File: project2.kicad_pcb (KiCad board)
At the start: 2 copper layers, 15 parts, among them J1 USB_C_Receptacle_PowerOnly_6P, Q1 FS8205A, Q2 DW01A, U1 TP4056-42-ESOP8

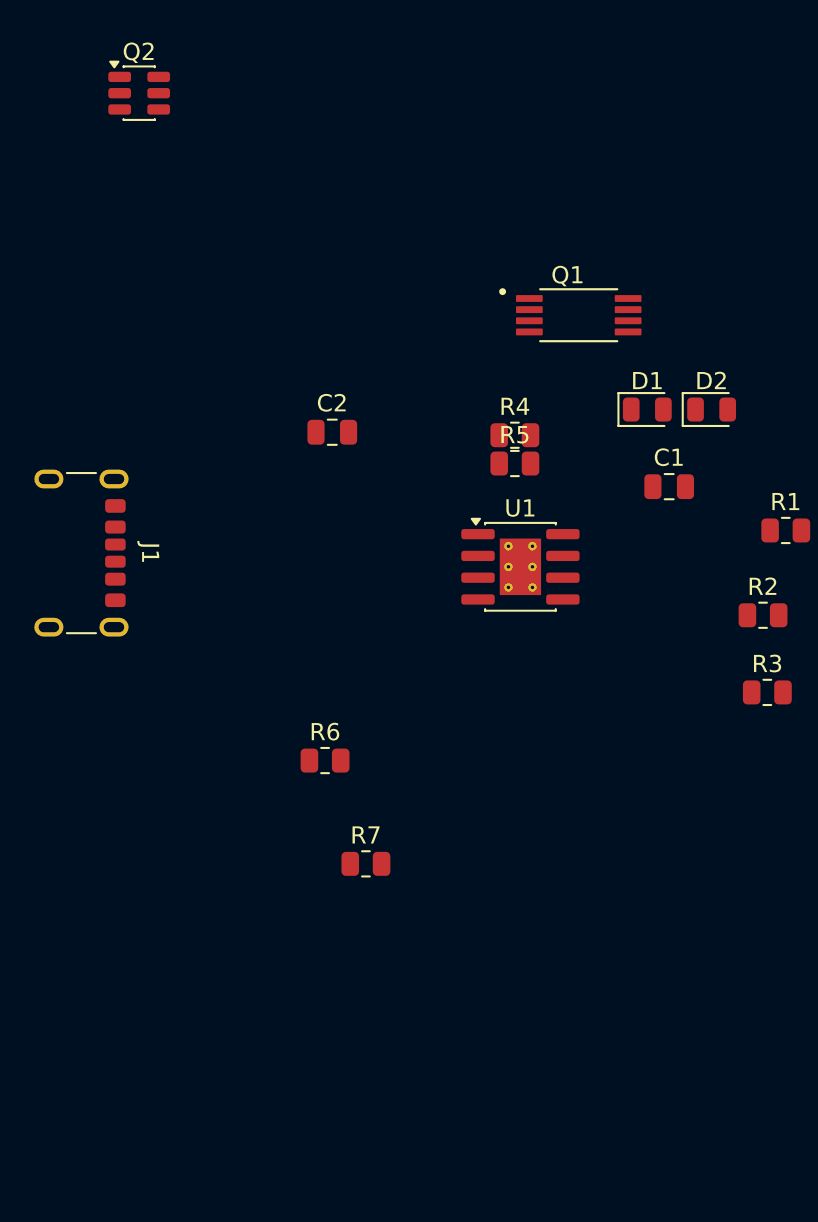
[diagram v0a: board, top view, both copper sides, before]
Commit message: MT3608 added
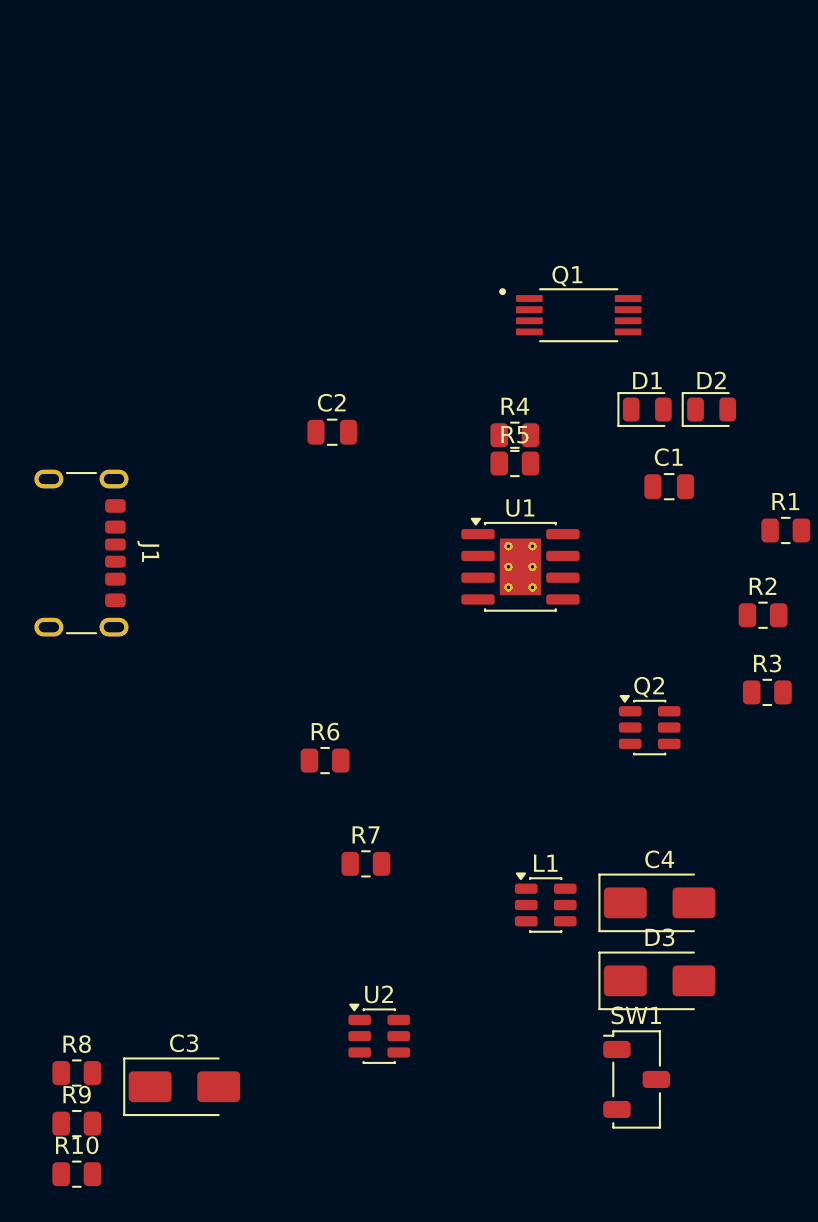
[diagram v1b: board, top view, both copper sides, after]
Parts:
- added C3: C, Diode_SMD:D_SMA, F.Cu at (29.5, 94.5)
- added C4: C, Diode_SMD:D_SMA, F.Cu at (57.2, 83.8)
- added D3: SS34, Diode_SMD:D_SMA, F.Cu at (57.2, 88.3)
- added L1: L, Package_TO_SOT_SMD:SOT-23-6, F.Cu at (50.6, 83.9)
- added R10: R, Resistor_SMD:R_0805_2012Metric, F.Cu at (23.2, 99.6)
- added R8: R, Resistor_SMD:R_0805_2012Metric, F.Cu at (23.2, 93.7)
- added R9: R, Resistor_SMD:R_0805_2012Metric, F.Cu at (23.2, 96.7)
- added SW1: SW_Nidec_CAS-120A1, Button_Switch_SMD:Nidec_Copal_CAS-120A, F.Cu at (55.9, 94.1)
- added U2: MT3608, Package_TO_SOT_SMD:SOT-23-6, F.Cu at (40.9, 91.5)
- moved Q2 47.5 mm to (56.6, 73.5)

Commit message: PCB created
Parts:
- added J2: Conn_01x01_Socket, Connector_Wire:SolderWirePad_1x01_SMD_1.5x3mm, F.Cu at (220.8, 99.6)
- added J3: Conn_01x01_Socket, Connector_Wire:SolderWirePad_1x01_SMD_1.5x3mm, F.Cu at (220.8, 92.8)
- added J4: Conn_01x01_Socket, Connector_Wire:SolderWirePad_1x01_SMD_1.5x3mm, F.Cu at (220.8, 106.3)
- added J5: Conn_01x01_Socket, Connector_Wire:SolderWirePad_1x01_SMD_1.5x3mm, F.Cu at (220.8, 113.0)
- L1: value L -> 22uH; footprint Package_TO_SOT_SMD:SOT-23-6 -> Inductor_SMD:L_7.3x7.3_H4.5
- R10: value R -> 16k
- R8: value R -> 2.2k
- R9: value R -> 42k
- moved R10 194.3 mm to (217.1, 113.4), turned to 180 degrees
- moved R8 190.7 mm to (213.3, 108.7), turned to 90 degrees
- moved R9 187.7 mm to (210.5, 108.7), turned to 90 degrees
- moved C3 182.0 mm to (211.2, 104.9)
- moved J1 177.0 mm to (195.0, 102.9)
- moved U2 177.0 mm to (217.0, 109.4), turned to -90 degrees
- moved C2 167.8 mm to (200.6, 98.1), turned to 90 degrees
- moved L1 164.5 mm to (214.7, 94.8)
- moved R4 161.6 mm to (201.8, 108.5), turned to 180 degrees
- moved C4 161.4 mm to (217.5, 102.9), turned to 90 degrees
- moved U1 159.9 mm to (204.6, 101.6), turned to -90 degrees
- moved R5 158.4 mm to (200.6, 103.2), turned to 90 degrees
- moved R7 158.2 mm to (197.9, 92.5)
- moved Q1 158.0 mm to (197.4, 112.5)
- moved R6 157.6 mm to (194.4, 92.5)
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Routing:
- net GND: track 0.00 -> 113.3 mm, vias 0 -> 5
- net Net-(D1-A): track 0.00 -> 51.9 mm
- net /BAT+: track 0.00 -> 39.4 mm, vias 0 -> 4
- net Net-(Q2-VCC): track 0.00 -> 25.6 mm, vias 0 -> 2
- net /OUT+: track 0.00 -> 25.2 mm
- net Net-(D3-A): track 0.00 -> 25.1 mm, vias 0 -> 2
- net Net-(U1-~{CHRG}): track 0.00 -> 19.3 mm, vias 0 -> 2
- net Net-(J1-CC1): track 0.00 -> 19.0 mm, vias 0 -> 2
- net Net-(U2-FB): track 0.00 -> 17.5 mm
- net Net-(U1-~{STDBY}): track 0.00 -> 17.1 mm, vias 0 -> 2
- net Net-(J1-CC2): track 0.00 -> 14.1 mm, vias 0 -> 2
- net Net-(Q1-G1): track 0.00 -> 11.7 mm
- net Net-(Q1-G2): track 0.00 -> 9.85 mm, vias 0 -> 2
- net Net-(SW1-A): track 0.00 -> 7.87 mm
- net Net-(Q2-CS): track 0.00 -> 7.73 mm
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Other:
- board outline added: 30 x 25 mm
